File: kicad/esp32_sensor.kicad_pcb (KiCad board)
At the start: 2 copper layers, 58.5 x 61.2 mm, 47 parts

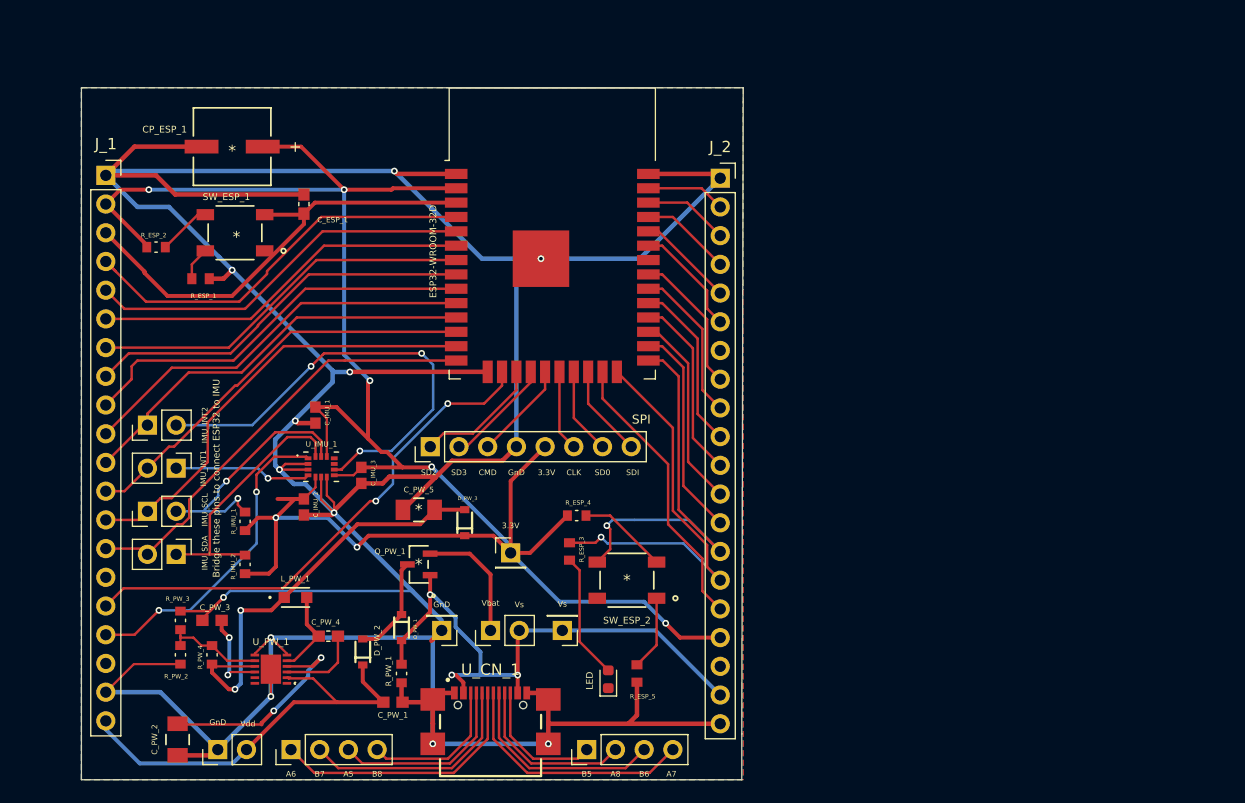
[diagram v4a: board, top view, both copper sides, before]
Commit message: Updated PCB to v0.0.3b. Fixed tracks and silkscreen.
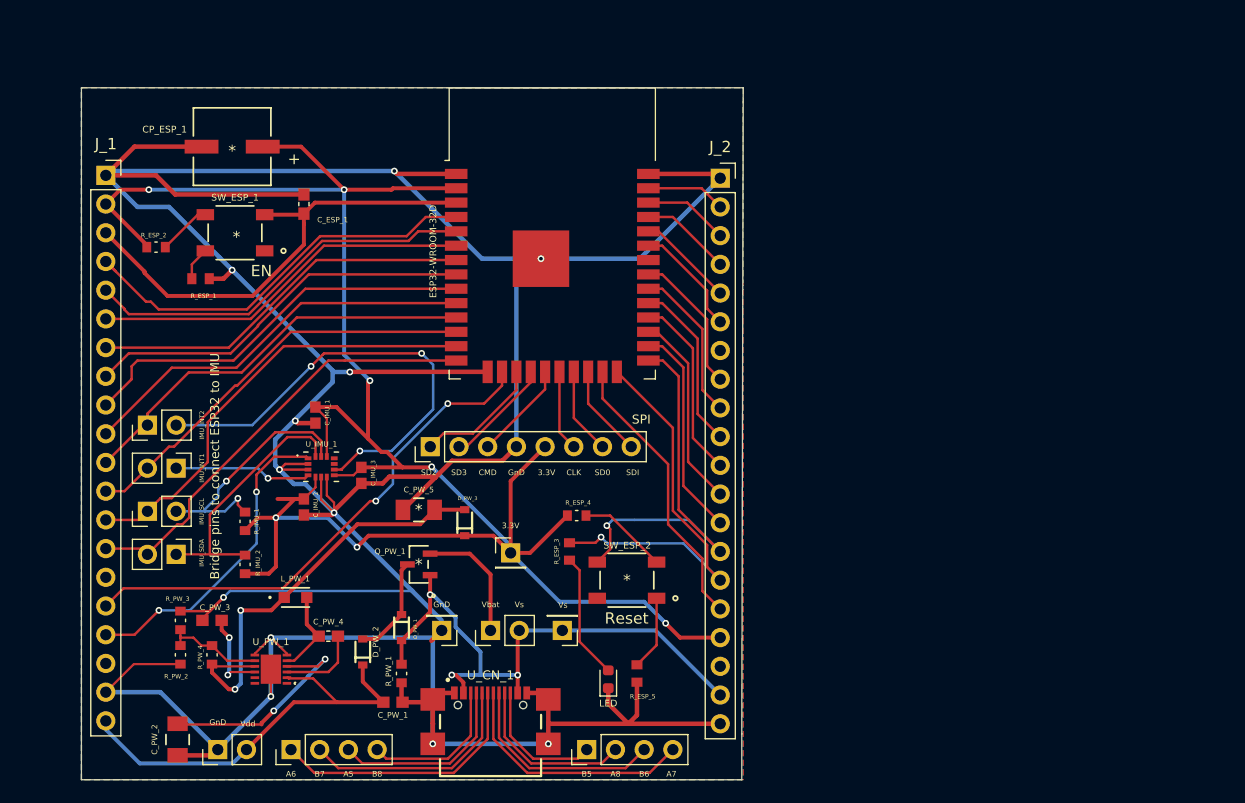
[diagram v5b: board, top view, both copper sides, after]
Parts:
- J_4: value Header_Pin_2 -> IMU_INT2
- J_5: value Header_Pin_2 -> IMU_INT1
- J_6: value Header_Pin_2 -> IMU_SCL
- J_7: value Header_Pin_2 -> IMU_SDA
- J_CN_3: value Vs -> Header_Pin_1
- J_CN_4: value GnD -> Header_Pin_1
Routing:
- net GND: track 372.6 -> 376.4 mm
- net /ESP32 Chip/ESP32_EN: track 41.0 -> 42.0 mm
- net Net-(C_PW_2-Pad1): track 18.7 -> 19.2 mm
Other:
- board text added: "Bridge pins to connect ESP32 to IMU"
- board text added: "ESP32 Sensor Module v0.0.3b"
- board text removed: "Bridge these pins to connect ESP32 to IMU"
- board text removed: "ESP32 Sensor Module v0.0.3"

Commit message: Re-exported KiCAD PCB files for assembly house/manufacturing. Updated README.md. Included BOM list
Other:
- board text added: "ESP32 Sensor Module v0.0.3c"
- board text added: "Published on 31 March 2021"
- board text removed: "ESP32 Sensor Module v0.0.3b"
- board text removed: "Published on 25 November 2020"
